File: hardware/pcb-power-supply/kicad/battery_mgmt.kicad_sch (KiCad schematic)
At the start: 21 parts, among them J1 Conn_01x02, Q1 PMOS, U3 BQ24195RGET

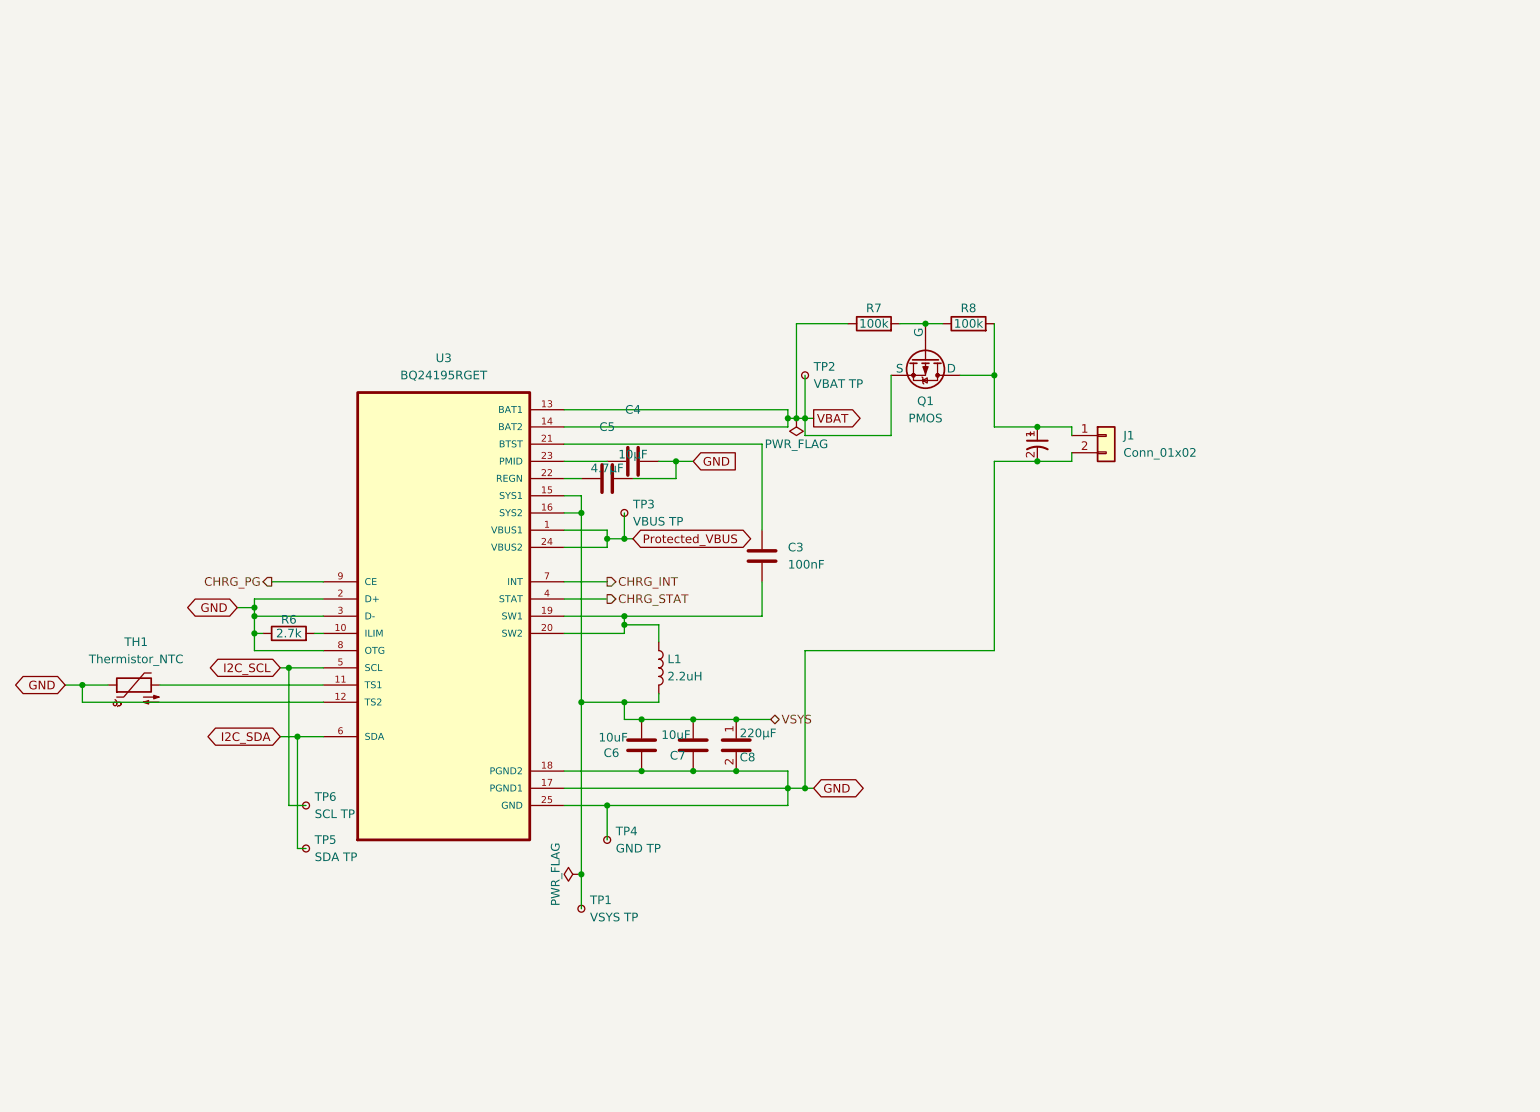
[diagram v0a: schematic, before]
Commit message: Add circuit-context.json for power supply PCB
Extract and annotate schematic context for the power supply board
(50 components, 29 nets, 4 functional blocks across 5 sheets).
Covers USB PD negotiation (STUSB4500), battery management (BQ24195),
power distribution (MT3608 boost + LR1801 LDO), and output connectors.

Creates power-schematic-context initiative docs (BRIEF/PLAN/TASKS).
Component ai_ annotations written to .kicad_sch files via annotate.py;
net/block annotations stored in circuit-context.json.

Made-with: Cursor
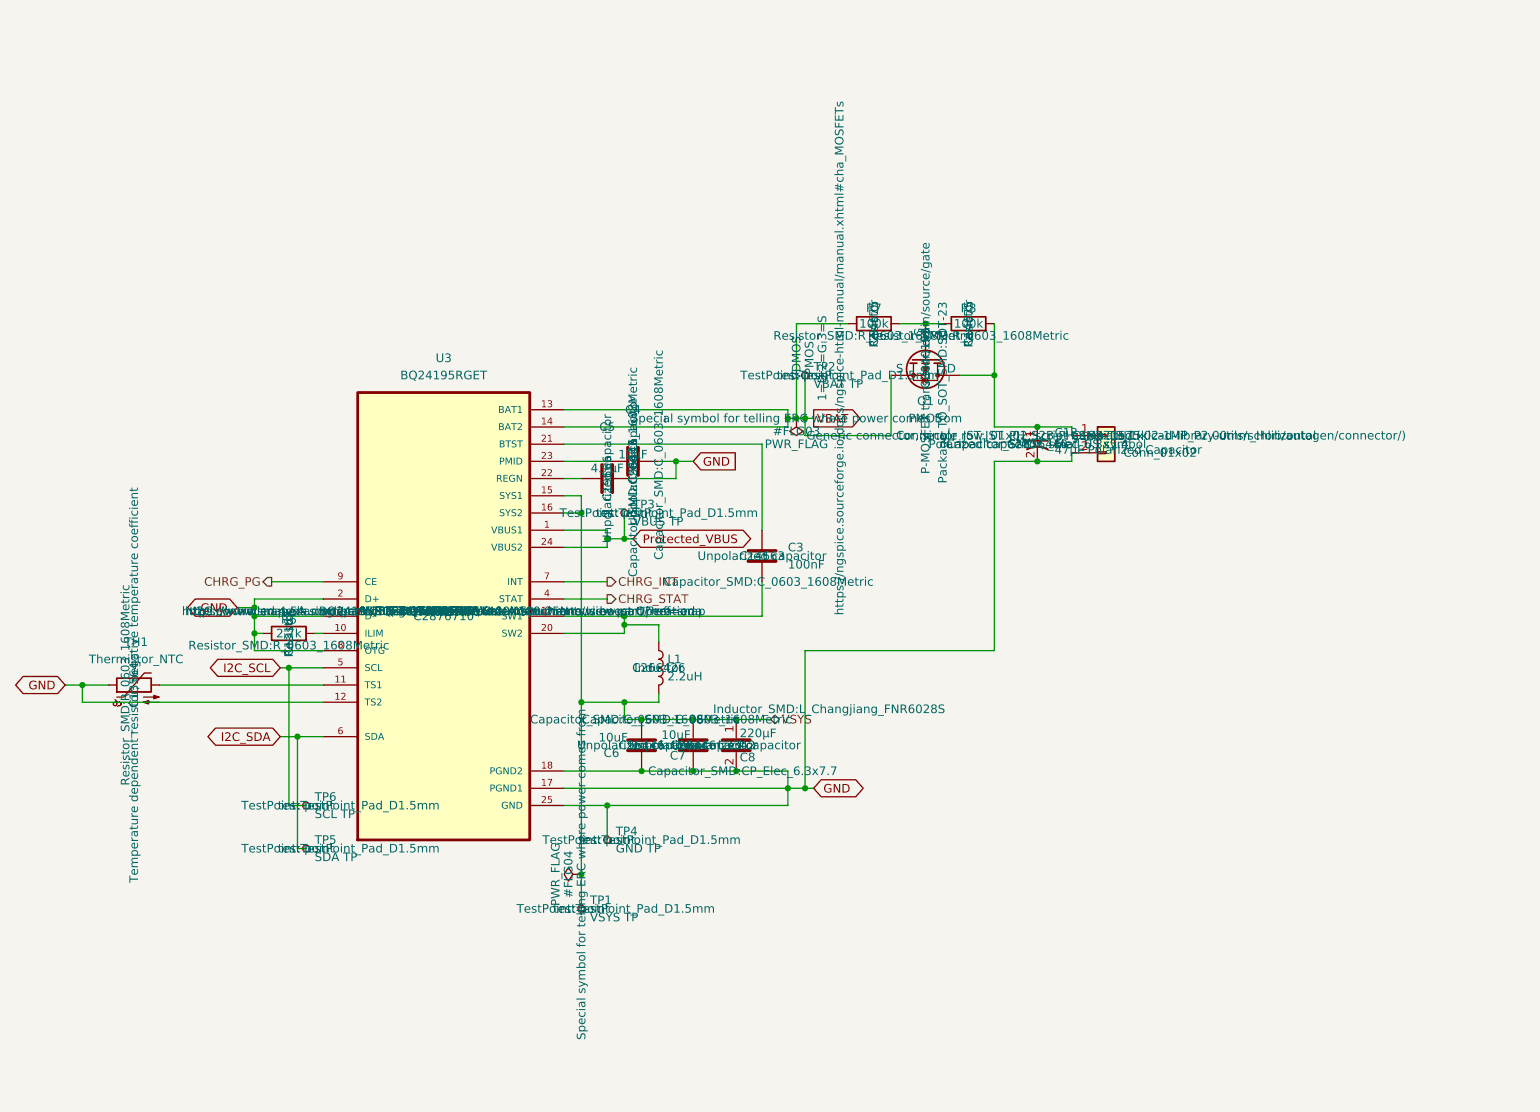
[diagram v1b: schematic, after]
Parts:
- C13: ai_block (none) -> battery_mgmt; ai_critical_specs (none) -> 47uF electrolytic; ai_function (none) -> Battery terminal bulk capacitor; ai_role (none) -> bulk_decoupling
- C3: ai_block (none) -> battery_mgmt; ai_critical_specs (none) -> 100nF; ai_function (none) -> BQ24195 bootstrap capacitor, BTST to SW; ai_role (none) -> bootstrap
- C4: ai_block (none) -> battery_mgmt; ai_critical_specs (none) -> 10uF ceramic; ai_function (none) -> BQ24195 PMID bypass capacitor; ai_role (none) -> bypass
- C5: ai_block (none) -> battery_mgmt; ai_critical_specs (none) -> 4.7uF ceramic; ai_function (none) -> BQ24195 REGN internal regulator capacitor; ai_role (none) -> bypass
- C6, C7: ai_block (none) -> battery_mgmt; ai_critical_specs (none) -> 10uF ceramic; ai_function (none) -> VSYS output decoupling capacitor; ai_role (none) -> decoupling
- C8: ai_block (none) -> battery_mgmt; ai_critical_specs (none) -> 220uF electrolytic; ai_function (none) -> VSYS bulk output capacitor; ai_role (none) -> bulk_decoupling
- J1: ai_block (none) -> battery_mgmt; ai_critical_specs (none) -> 2mm pitch; ai_function (none) -> Li-ion battery connector, JST PH 2-pin; ai_role (none) -> connector
- L1: ai_block (none) -> battery_mgmt; ai_critical_specs (none) -> 2.2uH FNR6028S; ai_function (none) -> BQ24195 switching inductor; ai_role (none) -> inductor
- Q1: ai_block (none) -> battery_mgmt; ai_critical_specs (none) -> SOT-23 PMOS; ai_function (none) -> Battery reverse polarity protection PMOS switch; ai_role (none) -> protection
- R6: ai_block (none) -> battery_mgmt; ai_critical_specs (none) -> 2.7k to GND; ai_function (none) -> BQ24195 ILIM input current limit setting resistor; ai_role (none) -> current_limit
- R7: ai_block (none) -> battery_mgmt; ai_critical_specs (none) -> 100k; ai_function (none) -> PMOS gate bias pull-up to VBAT; ai_role (none) -> bias
- R8: ai_block (none) -> battery_mgmt; ai_critical_specs (none) -> 100k; ai_function (none) -> PMOS gate bias to raw battery terminal; ai_role (none) -> bias
- TH1: ai_block (none) -> battery_mgmt; ai_critical_specs (none) -> 10k NTC; ai_function (none) -> Battery NTC thermistor for temperature monitoring; ai_role (none) -> temperature_sense
- TP1: ai_block (none) -> battery_mgmt; ai_function (none) -> VSYS voltage test point; ai_role (none) -> test_point
- TP2: ai_block (none) -> battery_mgmt; ai_function (none) -> VBAT voltage test point; ai_role (none) -> test_point
- TP3: ai_block (none) -> battery_mgmt; ai_function (none) -> Protected_VBUS voltage test point; ai_role (none) -> test_point
- TP4: ai_block (none) -> battery_mgmt; ai_function (none) -> Ground test point; ai_role (none) -> test_point
- TP5: ai_block (none) -> battery_mgmt; ai_function (none) -> I2C SDA test point; ai_role (none) -> test_point
- TP6: ai_block (none) -> battery_mgmt; ai_function (none) -> I2C SCL test point; ai_role (none) -> test_point
- U3: ai_block (none) -> battery_mgmt; ai_critical_specs (none) -> 4.5A input, 2A charge, integrated FETs, I2C configurable; ai_function (none) -> Li-ion battery charger and power path management IC; ai_role (none) -> charger_ic
